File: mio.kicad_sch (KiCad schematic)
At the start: 8 parts, among them U201 xc7z010clg400, U701 33.3333MHz

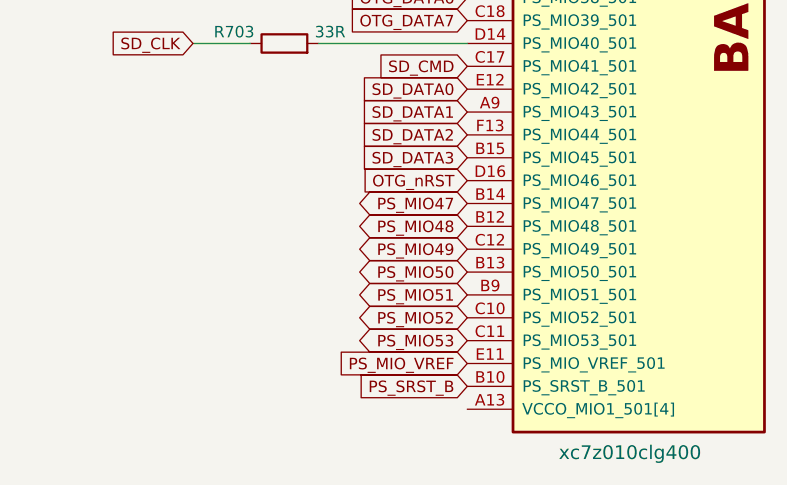
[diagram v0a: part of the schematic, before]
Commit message: layout: route mio and some io
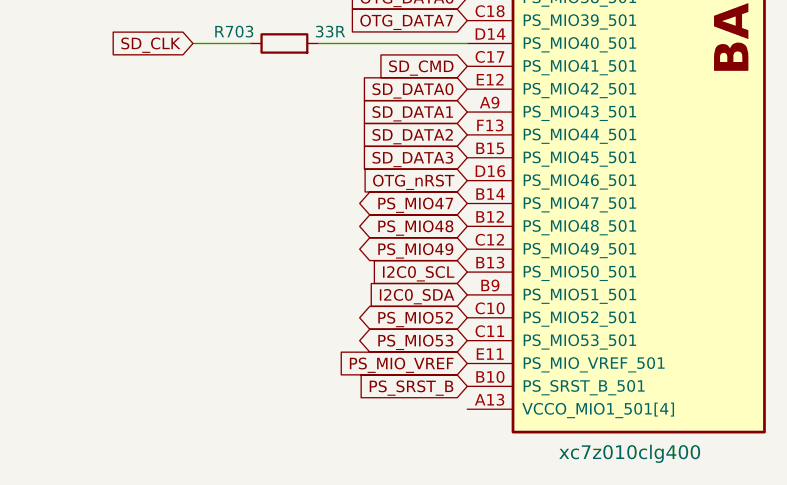
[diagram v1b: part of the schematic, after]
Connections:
- net PS_MIO50 renamed I2C0_SCL
- net PS_MIO51 renamed I2C0_SDA
